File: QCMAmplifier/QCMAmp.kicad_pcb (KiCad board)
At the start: 2 copper layers, 135 x 85 mm, 55 parts, among them J1 Screw_Terminal_01x02, J2 Screw_Terminal_01x02, J3 Screw_Terminal_01x02, J4 Screw_Terminal_01x02, J5 Screw_Terminal_01x02, J6 Screw_Terminal_01x02, J7 Screw_Terminal_01x02, J8 Screw_Terminal_01x02, J9 Screw_Terminal_01x02, U1 PA119CE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

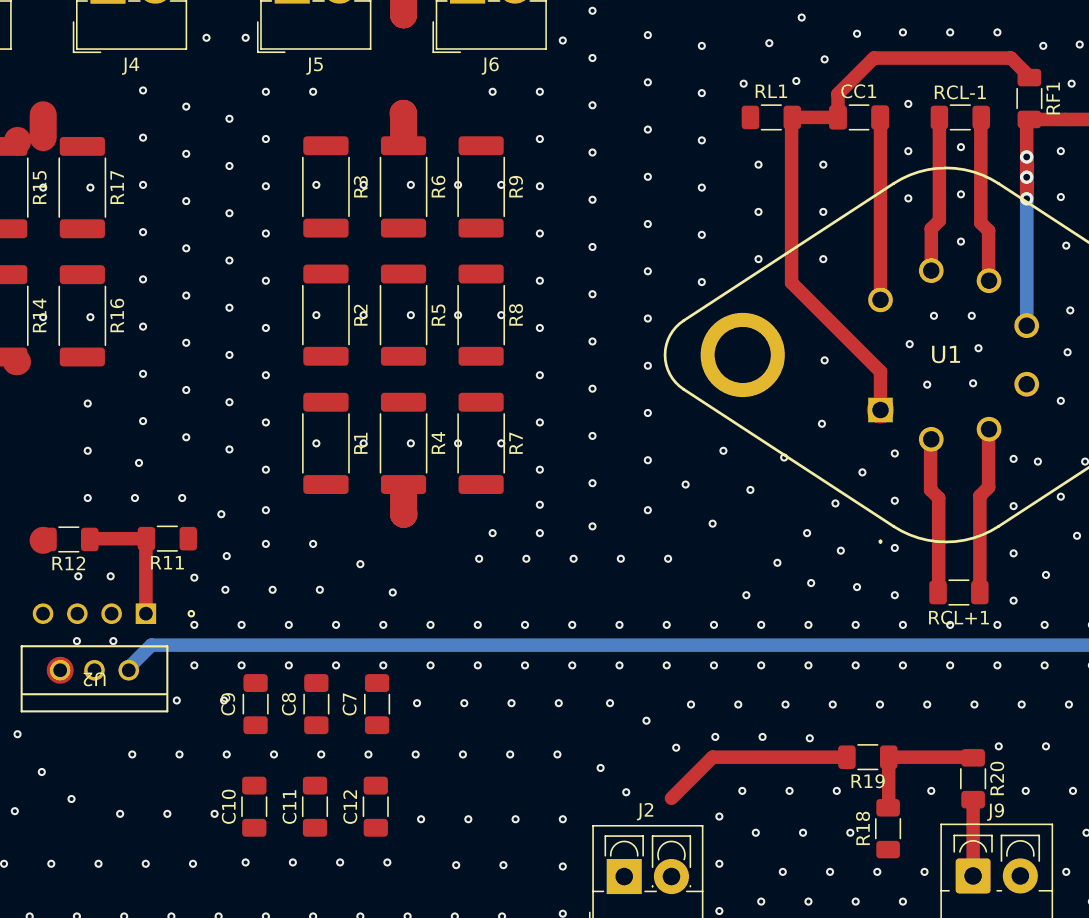
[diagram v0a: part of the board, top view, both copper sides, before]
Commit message: changes in schematic
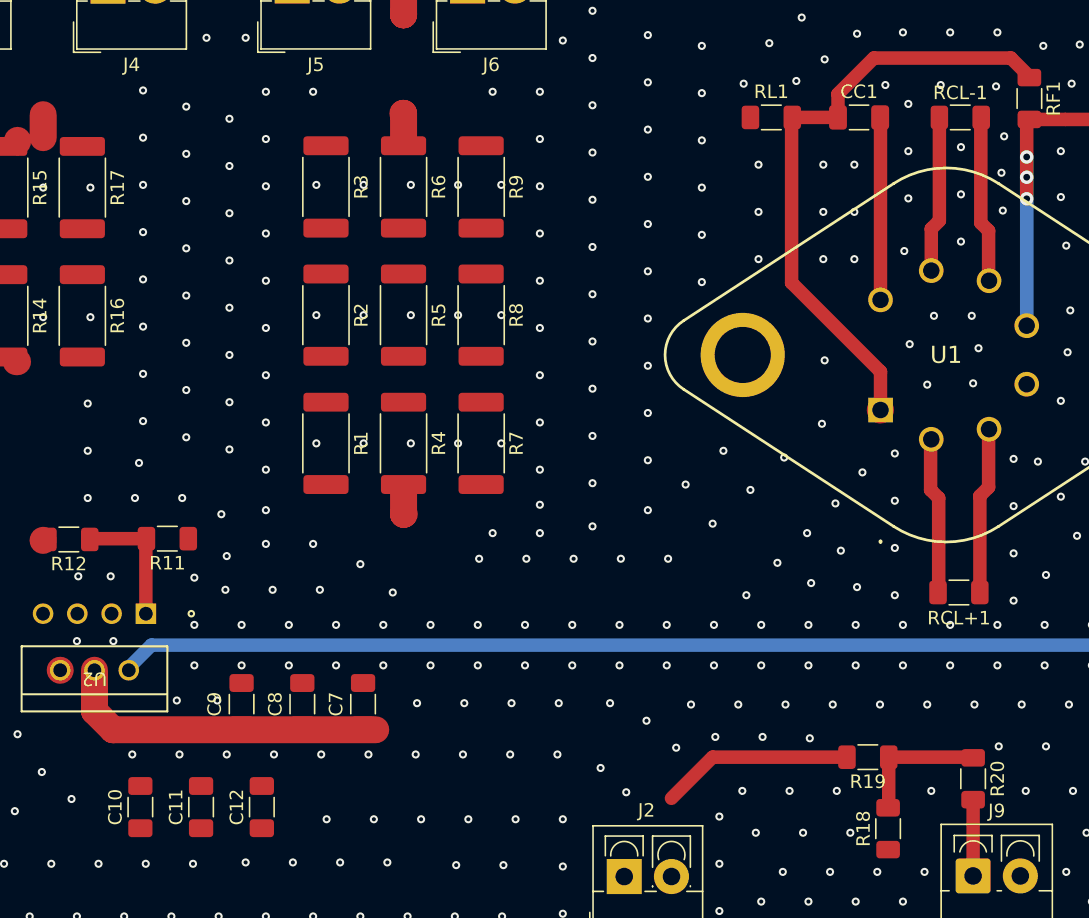
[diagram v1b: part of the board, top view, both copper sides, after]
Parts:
- C1, C12, C6, C9: value C -> 10uF
- C10, C3, C4, C7: value C -> 1nF
- C11, C2, C5, C8: value C -> 100nF
- moved C10 8.44 mm to (95.6, 113.0)
- moved C11 8.44 mm to (100.1, 113.0)
- moved C12 8.44 mm to (104.6, 113.0)
- moved C7 1.04 mm to (112.1, 105.4)
- moved C8 1.04 mm to (107.6, 105.4)
- moved C9 1.04 mm to (103.1, 105.4)
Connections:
- net /VS1+ renamed +36V
- net /VS1- renamed -36V
- net /VS2+ renamed +15V
- net /VS2- renamed -15V
- CC1 pad 1: /OUT_PA -> /OUT_PA_R
- J3 pad 2: /OUT -> /OUT_LT
- J4 pad 1: /OUT -> /OUT_LT
- J5 pad 2: /OUT -> /OUT_PA
- J6 pad 1: /OUT -> /OUT_PA
- R1 pad 2: /OUT_PA -> /OUT_PA_R
- R12 pad 2: /OUT_LT -> /OUT_LT_R
- R14 pad 2: /OUT_LT -> /OUT_LT_R
- R15 pad 1: /OUT -> /OUT_LT
- R16 pad 2: /OUT_LT -> /OUT_LT_R
- R17 pad 1: /OUT -> /OUT_LT
- R3 pad 1: /OUT -> /OUT_PA
- R4 pad 2: /OUT_PA -> /OUT_PA_R
- R6 pad 1: /OUT -> /OUT_PA
- R7 pad 2: /OUT_PA -> /OUT_PA_R
- R9 pad 1: /OUT -> /OUT_PA
- RF1 pad 1: /OUT_PA -> /OUT_PA_R
- RL1 pad 1: /OUT_PA -> /OUT_PA_R
- U1 pad 1: /OUT_PA -> /OUT_PA_R
- U2 pad 7: /OUT_LT -> /OUT_LT_R
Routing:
- net /OUT_PA_R: track 0.00 -> 110.0 mm
- net /OUT: track 83.3 -> 0.00 mm
- net /OUT_PA: track 110.0 -> 45.3 mm
- net /OUT_LT_R: track 0.00 -> 31.3 mm
- net /OUT_LT: track 31.3 -> 38.0 mm
- net GND: vias 649 -> 658

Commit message: changes made, gerbers added
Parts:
- added H4: MountingHole, MountingHole:MountingHole_3.2mm_M3, F.Cu at (191.4, 62.9)
- added H5: MountingHole, MountingHole:MountingHole_3.2mm_M3, F.Cu at (139.0, 106.0)
- added H6: MountingHole, MountingHole:MountingHole_3.2mm_M3, F.Cu at (164.0, 51.0)
- added H7: MountingHole, MountingHole:MountingHole_3.2mm_M3, F.Cu at (139.0, 51.0)
- added H8: MountingHole, MountingHole:MountingHole_3.2mm_M3, F.Cu at (164.0, 106.0)
- J7: footprint TerminalBlock_4Ucon:TerminalBlock_4Ucon_1x02_P3.50mm_Vertical -> Connector_Coaxial:SMA_Amphenol_132134_Vertical
- moved H3 63.2 mm to (78.4, 62.9)
- moved C4 11.5 mm to (170.6, 98.4)
- moved C5 11.5 mm to (170.6, 102.9)
- moved C6 11.5 mm to (170.6, 107.4)
- moved C1 10.3 mm to (180.8, 107.4)
- moved C2 10.3 mm to (180.8, 102.9)
- moved C3 10.3 mm to (180.8, 98.4)
- moved J1 10.2 mm to (172.5, 118.1)
- moved R13 9.39 mm to (183.8, 74.9)
- moved D1 9.37 mm to (184.2, 62.8)
- moved J8 9.36 mm to (186.8, 52.2)
- moved JP2 9.30 mm to (182.2, 69.5)
- moved H2 8.25 mm to (191.4, 121.9)
- moved J7 7.91 mm to (175.2, 52.2)
- moved R20 6.04 mm to (151.3, 110.6), turned to 0 degrees
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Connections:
- J7 pad 1: GND -> /IN
- J7 pad 2: /IN -> GND
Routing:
- net GND: track 0.00 -> 19.7 mm, vias 658 -> 580
- net +36V: track 66.4 -> 54.0 mm
- net +15V: track 70.2 -> 63.7 mm
- net Net-(JP1-B): track 13.0 -> 7.92 mm
- net -36V: track 80.0 -> 75.5 mm
- net /IN: track 39.2 -> 35.8 mm
- net Net-(R18-Pad2): track 10.0 -> 6.75 mm
- net Net-(U1--IN): track 23.9 -> 21.7 mm
- net Net-(J9-Pin_1): track 5.65 -> 7.49 mm
- net Net-(JP2-B): track 113.6 -> 112.2 mm
- net Net-(U1-CC): track 13.5 -> 12.7 mm
- net Net-(U1--CL): track 11.4 -> 10.8 mm
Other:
- board size 135 x 85 mm -> 125 x 85 mm
- board text added: "JLCJLCJLCJLC"
